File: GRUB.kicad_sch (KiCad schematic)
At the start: 40 parts, among them J2 External Digital Controller, J3 Timer or foot switch, Q1 2N3904, Q2 2N3904, Q3 2N3904, Q5 2N3904, SW1 Red, SW2 UV, SW3 Blue, SW4 1) Focus 2) Safelight 3) RGB-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, SW6 Green, U1 A009 BuckBlock, U10 EL817, U11 EL817, U12 EL817, U2 A009 BuckBlock, U3 A009 BuckBlock, U4 EL817, U5 EL817, U6 A009 BuckBlock, U7 EL817, U8 EL817, U9 EL817

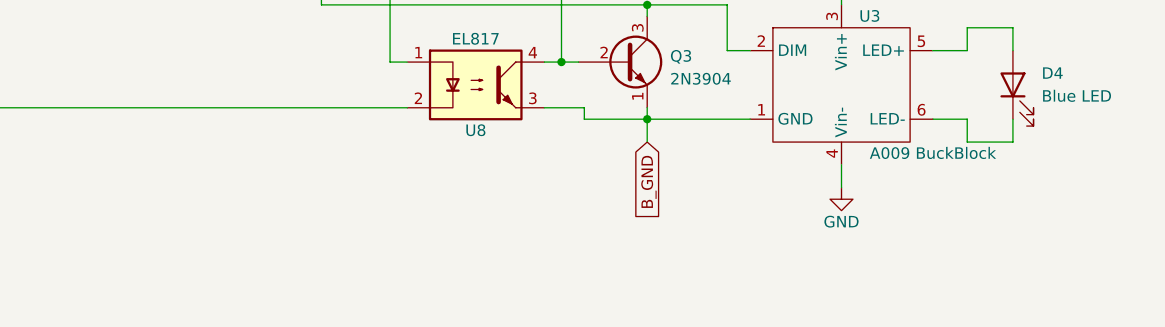
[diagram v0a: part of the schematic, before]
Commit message: Adding link to A009 datasheet
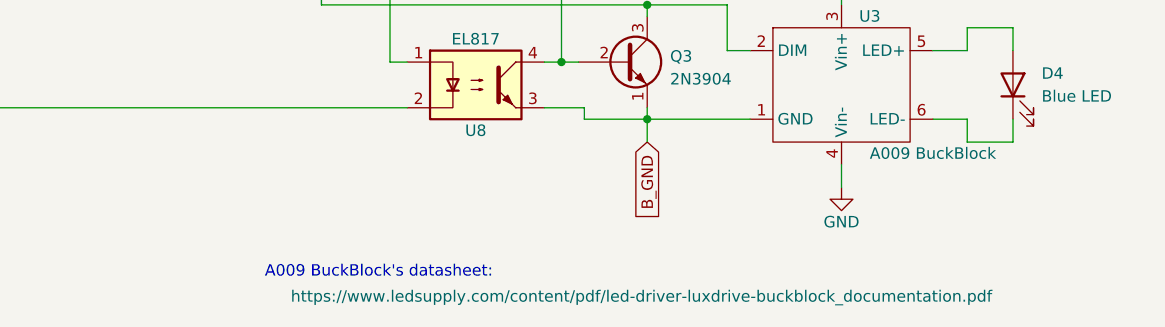
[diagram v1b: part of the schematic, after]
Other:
- note added: "A009 BuckBlock's datasheet:"
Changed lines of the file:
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@@
     (stroke (width 0) (type default))
+  )
+  (text "A009 BuckBlock's datasheet:" (at 206.375 168.91 0)
+    (effects (font (size 1.27 1.27)) (justify right bottom))
   )
   (text "GND" (at 31.115 97.155 0)
@@
       (effects (font (size 1.27 1.27)) hide)
     )
-    (property "Datasheet" "" (at 245.11 147.32 0)
-      (effects (font (size 1.27 1.27)) hide)
-    )
-    (pin "1")
+    (property "Datasheet" "https://www.ledsupply.com/content/pdf/led-driver-luxdrive-buckblock_documentation.pdf" (at 222.885 170.815 0)
+      (effects (font (size 1.27 1.27)))
+    )
+    (pin "1")

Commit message: Adding link to A009 datasheet
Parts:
- removed U10, U11, U12, U4, U5, U7, U8, U9: EL817, Package_DIP:DIP-4_W7.62mm, symbol Isolator:EL817
- added U13, U4: PC847, Housings_DIP:DIP-16_W7.62mm, symbol opto:PC847
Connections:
- net B_GND: now also U13.9, U4.9
- net G_GND: now also U13.15, U4.15
- net R_GND: now also U13.13, U4.13
- net U_GND: now also U13.11, U4.11
- net at J2.1 (Pin_1): now also U13.2
- net at J2.2 (Pin_2): now also U13.4
- net at J2.3 (Pin_3): now also U13.6
- net at J2.4 (Pin_4): now also U13.8
- net at J2.5 (Pin_5), J3.1 (Pin_1): now also U4.8
- net at R2.2: now also U13.1
- net at Q2.2 (B), R8.2: now also U4.12
- net at R11.1: now also U4.1
- net at Q5.2 (B), R1.2: now also U4.16
- net at R3.2: now also U13.3
- net at SW4.4: now also U13.14
- net at R5.2: now also U13.7
- net at SW4.10: now also U13.10
- net at SW4.1: now also U13.16
- net at SW4.7: now also U13.12
- net at Q3.2 (B), R9.2: now also U4.10
- net at R4.2: now also U13.5
- net at Q1.2 (B), R6.2: now also U4.14
- new net: U4.2, U4.3
- new net: U4.4, U4.5
- new net: U4.6, U4.7

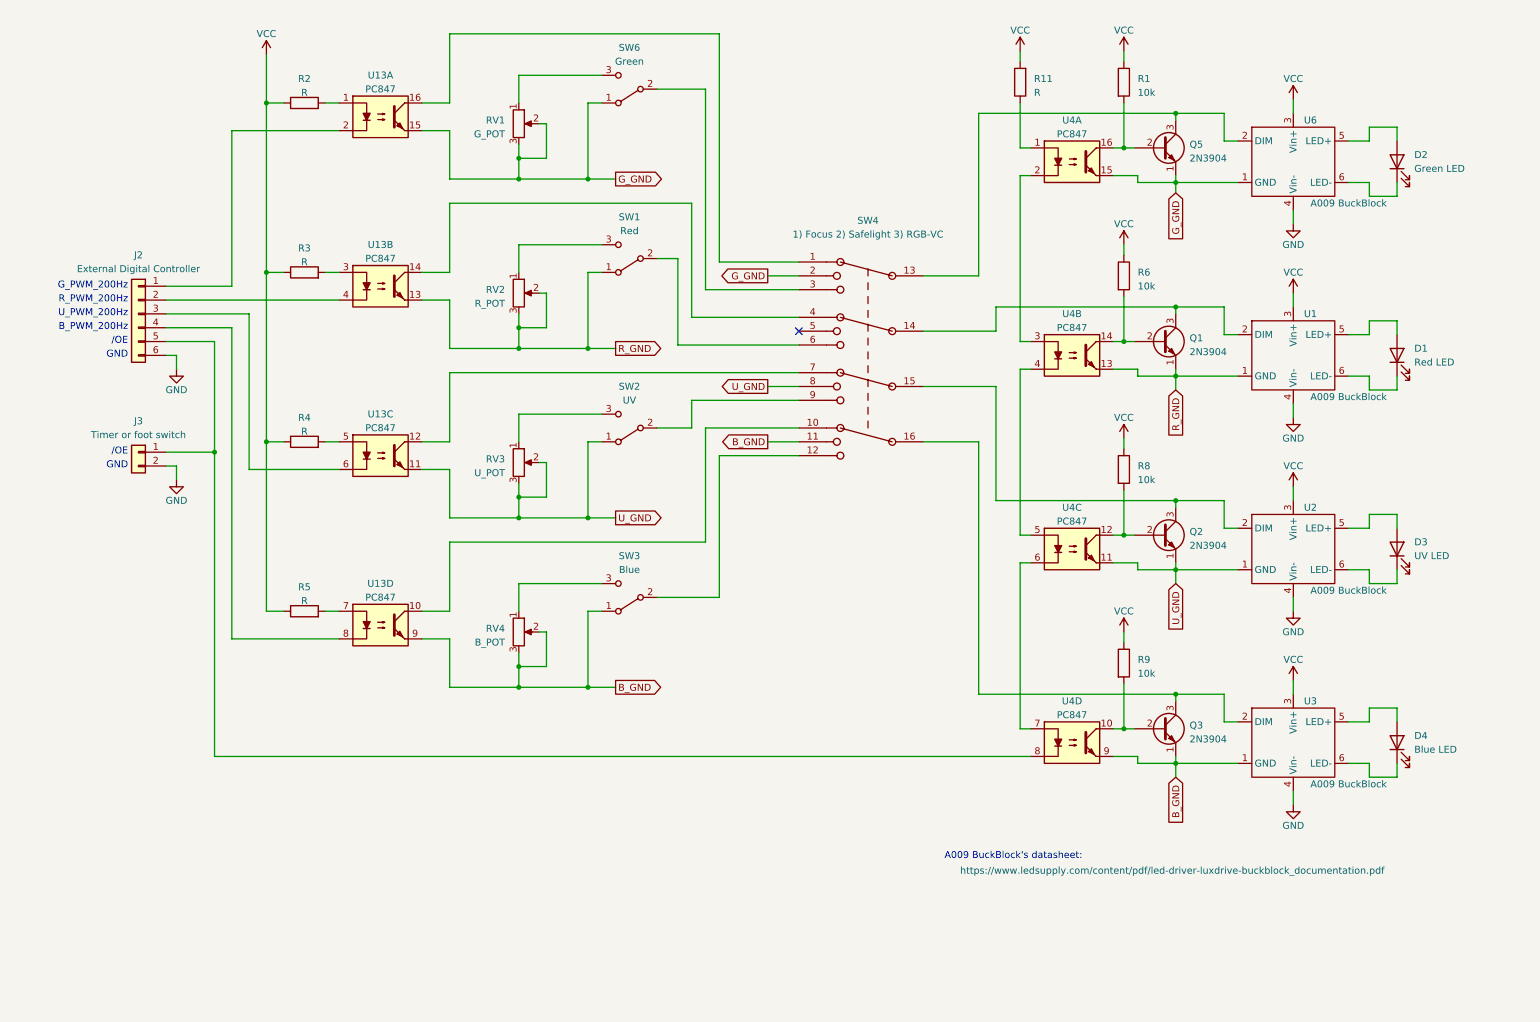
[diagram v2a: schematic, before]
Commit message: Adding option for LDDS-HWB LED driver
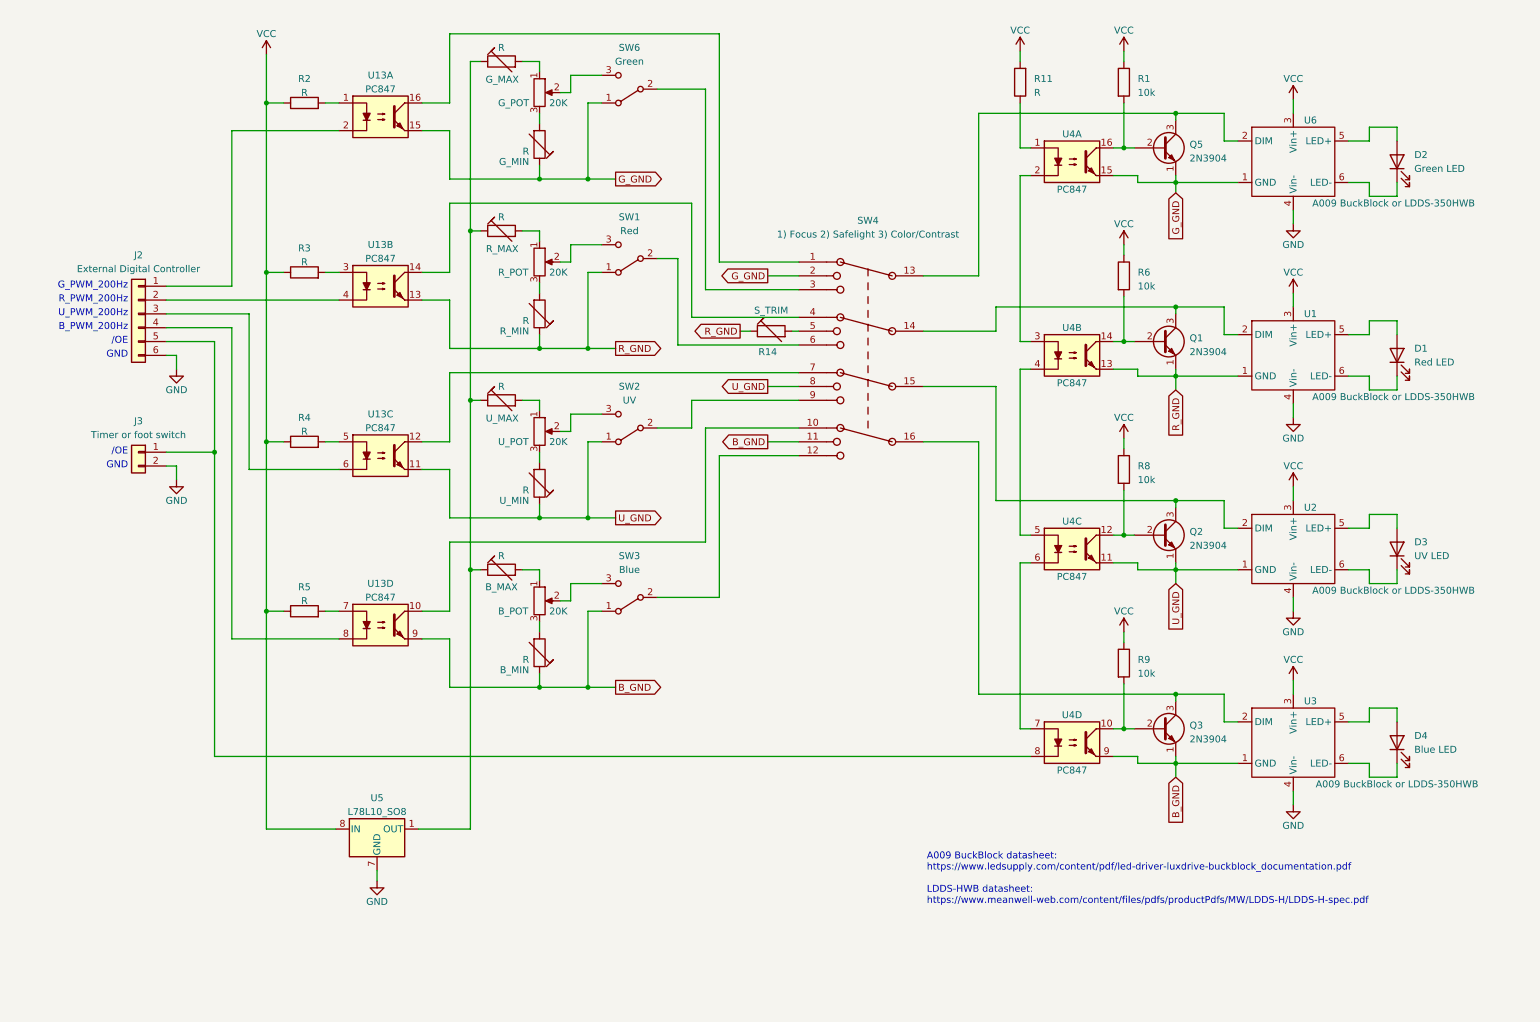
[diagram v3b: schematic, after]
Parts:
- removed RV1: G_POT, symbol Device:R_POT
- removed RV2: R_POT, symbol Device:R_POT
- removed RV3: U_POT, symbol Device:R_POT
- removed RV4: B_POT, symbol Device:R_POT
- added B_MAX, B_MIN, G_MAX, G_MIN, R_MAX, R_MIN, U_MAX, U_MIN: R, symbol Device:RTRIM
- added B_POT, G_POT, R_POT, U_POT: 20K, symbol Device:R_POT
- added R14: S_TRIM, symbol Device:RTRIM
- added U5: L78L10_SO8, Package_SO:SOIC-8_3.9x4.9mm_P1.27mm, symbol Regulator_Linear:L78L10_SO8
- SW4: value 1) Focus 2) Safelight 3) RGB-VC -> 1) Focus 2) Safelight 3) Color/Contrast
- U1, U2, U3, U6: value A009 BuckBlock -> A009 BuckBlock or LDDS-350HWB
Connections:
- net B_GND: now also B_MIN.1
- net GND: now also U5.2 (GND), U5.3 (GND), U5.6 (GND), U5.7 (GND)
- net G_GND: now also G_MIN.1
- net R_GND: now also R14.1, R_MIN.1
- net U_GND: now also U_MIN.1
- net VCC: now also U5.8 (IN)
- net at SW1.3 (C): now also R_POT.2
- net at SW3.3 (C): now also B_POT.2
- net at SW2.3 (C): now also U_POT.2
- net at SW6.3 (C): now also G_POT.2
- net at SW4.5: now also R14.2
- new net: B_MAX.1, G_MAX.1, R_MAX.1, U5.1 (OUT), U_MAX.1
- new net: U_MAX.2, U_POT.1
- new net: G_MAX.2, G_POT.1
- new net: G_MIN.2, G_POT.3
- new net: R_MIN.2, R_POT.3
- new net: U_MIN.2, U_POT.3
- new net: B_MIN.2, B_POT.3
- new net: B_MAX.2, B_POT.1
- new net: R_MAX.2, R_POT.1
- no-connect marks 1 -> 0
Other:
- note added: "A009 BuckBlock datasheet: https://www.ledsupply.com/content/pdf/led-driver-luxdrive-buckblock_documentation.pdf LDDS-HWB datasheet: https://www.meanwell-web.com/content/files/pdfs/productPdfs/MW/LDDS-H/LDDS-H-spec.pdf"
- note removed: "A009 BuckBlock's datasheet:"

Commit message: Changed the DIM control from potentiometer mode to voltage mode, added trimmers regulations description
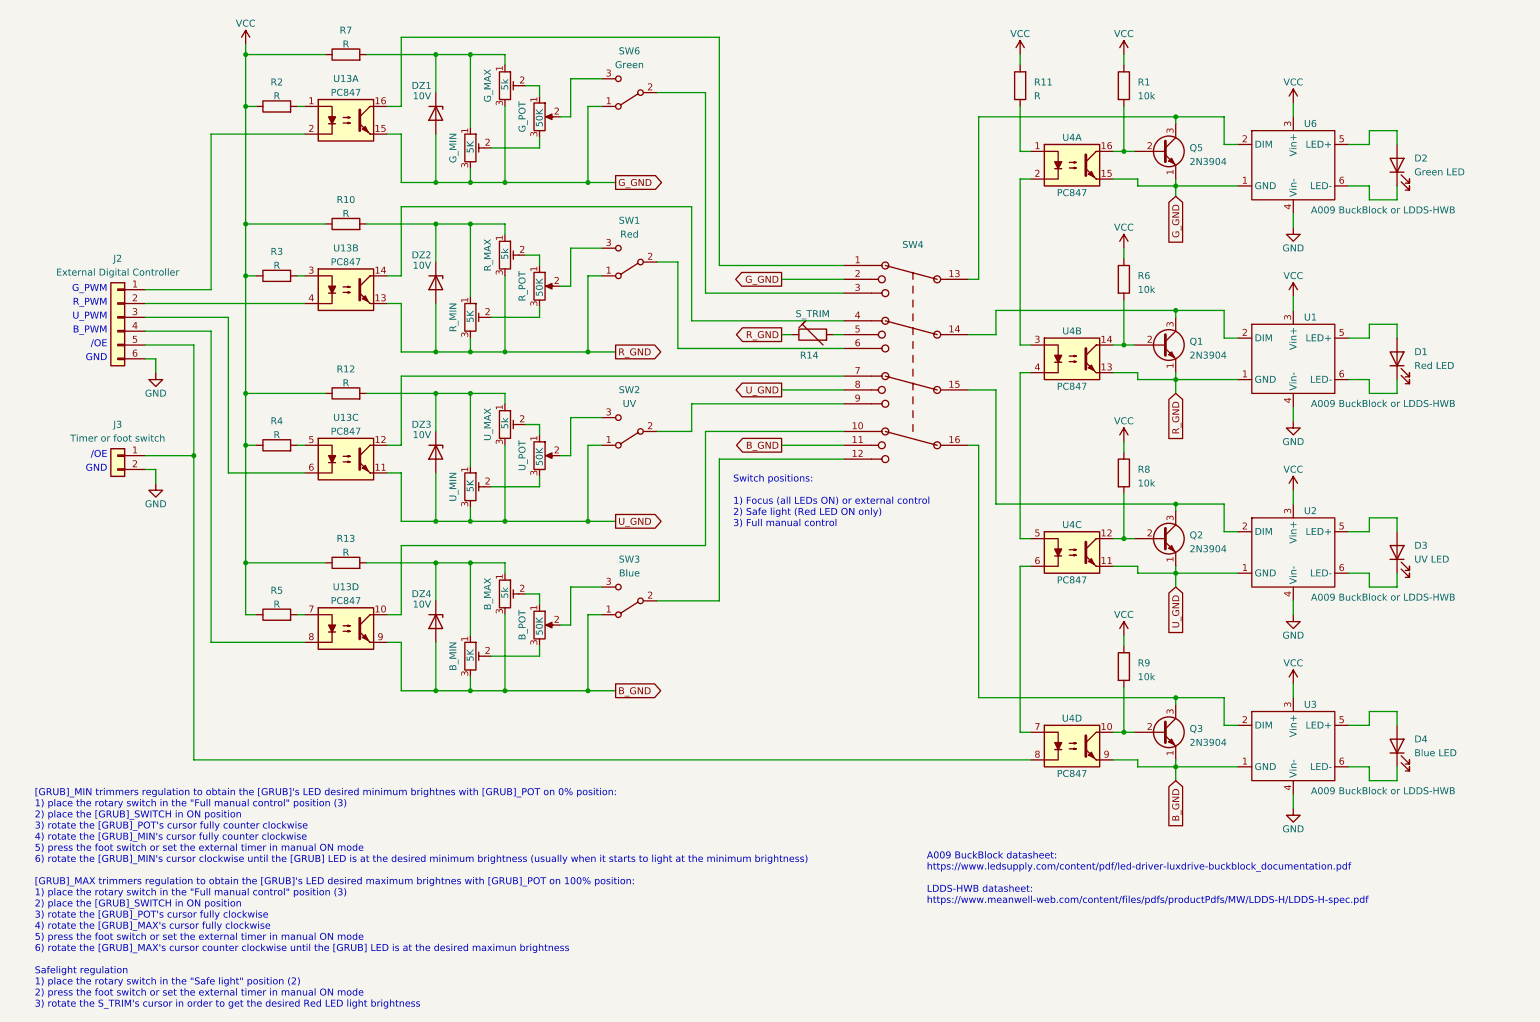
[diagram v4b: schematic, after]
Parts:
- removed B_MAX, B_MIN, G_MAX, G_MIN, R_MAX, R_MIN, U_MAX, U_MIN: R, symbol Device:RTRIM
- removed U5: L78L10_SO8, Package_SO:SOIC-8_3.9x4.9mm_P1.27mm, symbol Regulator_Linear:L78L10_SO8
- added B_MAX, G_MAX, R_MAX, U_MAX: 5k, symbol Device:R_POT_TRIM
- added B_MIN, G_MIN, R_MIN, U_MIN: 5K, symbol Device:R_POT_TRIM
- added DZ1, DZ2, DZ3, DZ4: 10V, Diode_SMD:D_SOD-523, symbol Diode:DZ2S100X0L
- added R10, R12, R13, R7: R, symbol device:R
- B_POT, G_POT, R_POT, U_POT: value 20K -> 50K
- U1, U2, U3, U6: value A009 BuckBlock or LDDS-350HWB -> A009 BuckBlock or LDDS-HWB
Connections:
- net B_GND: now also B_MAX.3, B_MIN.3, DZ4.2 (A)
- net G_GND: now also DZ1.2 (A), G_MAX.3, G_MIN.3
- net R_GND: now also DZ2.2 (A), R_MAX.3, R_MIN.3
- net U_GND: now also DZ3.2 (A), U_MAX.3, U_MIN.3
- net VCC: now also R10.1, R12.1, R13.1, R7.1
- net at U_POT.1: now also U_MAX.2
- net at G_POT.1: now also G_MAX.2
- net at G_POT.3: now also G_MIN.2
- net at R_POT.3: now also R_MIN.2
- net at U_POT.3: now also U_MIN.2
- net at B_POT.3: now also B_MIN.2
- net at B_POT.1: now also B_MAX.2
- net at R_POT.1: now also R_MAX.2
- new net: DZ1.1 (K), G_MAX.1, G_MIN.1, R7.2
- new net: DZ2.1 (K), R10.2, R_MAX.1, R_MIN.1
- new net: DZ3.1 (K), R12.2, U_MAX.1, U_MIN.1
- new net: B_MAX.1, B_MIN.1, DZ4.1 (K), R13.2
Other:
- note added: "B_PWM"
- note added: "G_PWM"
- note added: "R_PWM"
- note added: "Switch positions: 1) Focus (all LEDs ON) or external control 2) Safe light (Red LED ON only) 3) Full manual control"
- note added: "U_PWM"
- note added: "[GRUB]_MIN trimmers regulation to obtain the [GRUB]'s LED desired minimum brightnes with [GRUB]_POT on 0% position: 1) place the rotary switch in the "Full manual control" position (3) 2) place the [GRUB]_SWITCH in ON position 3) rotate the [GRUB]_POT's cursor fully counter clockwise 4) rotate the [GRUB]_MIN's cursor fully counter clockwise 5) press the foot switch or set the external timer in ma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"
- note removed: "B_PWM_200Hz"
- note removed: "G_PWM_200Hz"
- note removed: "R_PWM_200Hz"
- note removed: "U_PWM_200Hz"
- moved on the sheet: D1, D2, D3, D4, J2, J3, Q1, Q2, Q3, Q5, R1, R11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
